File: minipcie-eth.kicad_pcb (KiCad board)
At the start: 2 copper layers, 156 x 41 mm, 36 parts, among them J2 POE PMOD, U1 VoCore_v2, U2 si3404, U3 ap2112, U4 MPCIE-Socket, X1 SI-52003-F

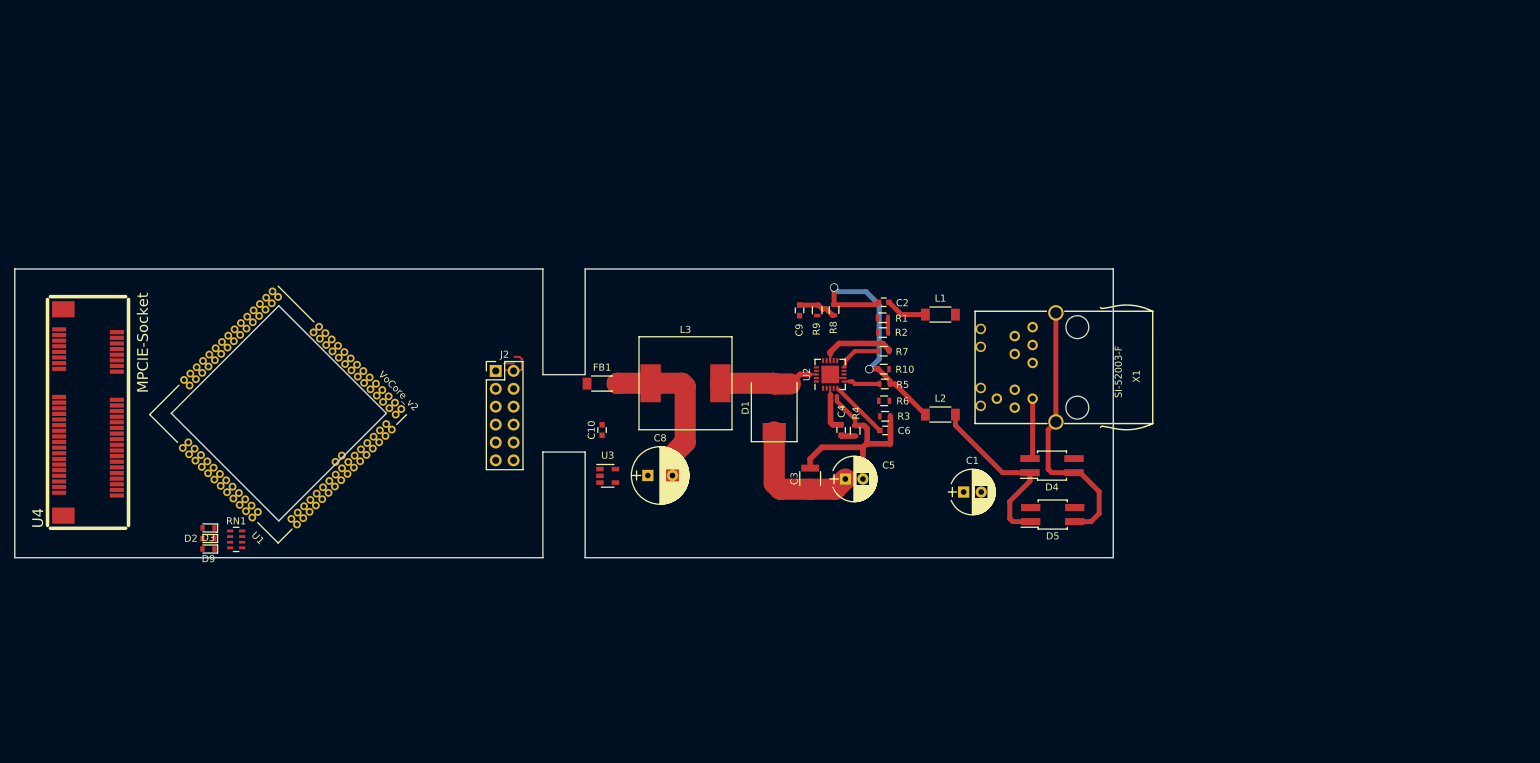
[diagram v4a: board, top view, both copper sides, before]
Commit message: Added PMOD 6 header pins, mouse bites, copper fills for main board
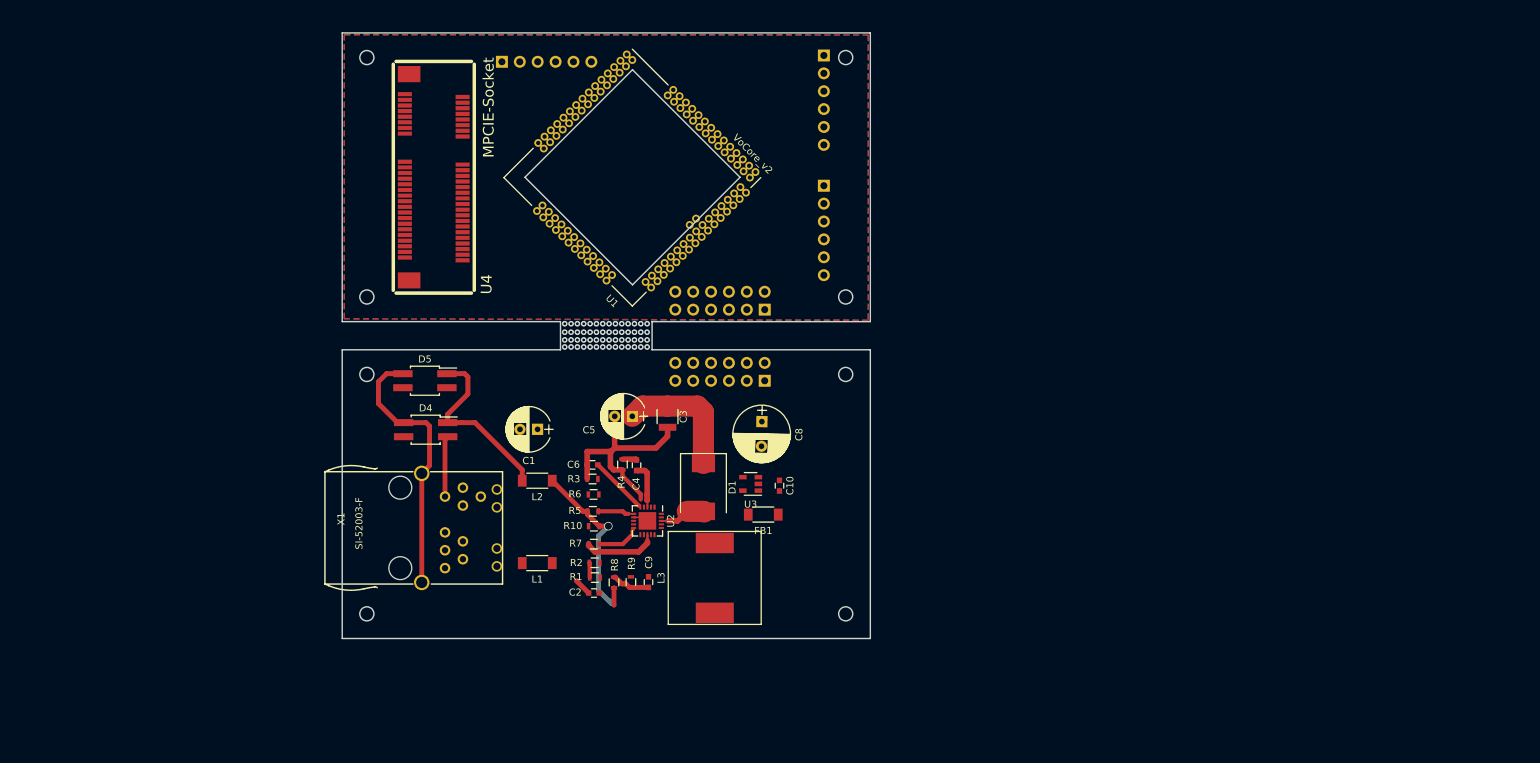
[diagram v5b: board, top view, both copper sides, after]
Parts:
- removed D2: TX, KiCad/Diodes_SMD.pretty:D_0603
- removed D3: PWR, KiCad/Diodes_SMD.pretty:D_0603
- removed D9: RX, KiCad/Diodes_SMD.pretty:D_0603
- removed RN1: RN_LEDS, KiCad/Resistors_SMD.pretty:R_Array_Concave_4x0603
- added J1: PoE connector MainBoard, Connector_PinHeader_2.54mm:PinHeader_2x06_P2.54mm_Vertical, B.Cu at (170.9, 86.7)
- added J3: PoE connector addon, Connector_PinHeader_2.54mm:PinHeader_2x06_P2.54mm_Vertical, B.Cu at (170.9, 96.8)
- added J4: PMOD UART 6pin, Connector_PinHeader_2.54mm:PinHeader_1x06_P2.54mm_Horizontal, B.Cu at (179.3, 50.6)
- added J5: PMOD UART 6pin, Connector_PinHeader_2.54mm:PinHeader_1x06_P2.54mm_Horizontal, B.Cu at (133.6, 51.5)
- J2: value POE PMOD -> PMOD I2C 6pin; footprint Connector_PinHeader_2.54mm:PinHeader_2x06_P2.54mm_Vertical -> Connector_PinHeader_2.54mm:PinHeader_1x06_P2.54mm_Horizontal; moved to B.Cu
- moved X1 92.9 mm to (122.2, 117.7), turned to 270 degrees
- moved D5 91.2 mm to (122.6, 96.8), turned to 0 degrees
- moved D4 89.1 mm to (122.7, 103.7), turned to 0 degrees
- moved L1 67.3 mm to (138.6, 122.7), turned to 180 degrees
- moved C1 61.2 mm to (138.6, 103.7), turned to 180 degrees
- moved U1 60.5 mm to (152.1, 68.0)
- moved U4 59.4 mm to (123.9, 55.4)
- moved C2 58.3 mm to (146.6, 126.9), turned to 180 degrees
- moved L2 58.0 mm to (138.6, 111.0), turned to 180 degrees
- moved R1 55.0 mm to (146.8, 124.7), turned to 180 degrees
- moved J2 53.5 mm to (179.3, 69.1), turned to 180 degrees
- moved R2 52.4 mm to (146.7, 122.6), turned to 180 degrees
- moved R8 49.7 mm to (149.5, 125.4), turned to 90 degrees
- moved R7 49.4 mm to (146.6, 120.0), turned to 180 degrees
- moved R10 46.8 mm to (146.6, 117.4), turned to 180 degrees
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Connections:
- C10 pad 1: +5V -> /ethernet + POE/5V+_POE
- C10 pad 2: GND -> /ethernet + POE/3V3-_POE
- C2 pad 1: +5V -> /ethernet + POE/5V+_POE
- C3 pad 1: +5V -> /ethernet + POE/5V+_POE
- C5 pad 1: +5V -> /ethernet + POE/5V+_POE
- C8 pad 1: +5V -> /ethernet + POE/5V+_POE
- C9 pad 2: GND -> /ethernet + POE/3V3-_POE
- D1 pad 1: +5V -> /ethernet + POE/5V+_POE
- FB1 pad 1: GND -> /ethernet + POE/3V3-_POE
- J2 pad 1: Net-(J2-Pad1) -> (no net)
- J2 pad 2: Net-(J2-Pad2) -> (no net)
- J2 pad 5: GNDA -> GND
- J2 pad 6: VBUS -> +3V3
- L2 pad 1: +5V -> /ethernet + POE/5V+_POE
- R10 pad 1: +5V -> /ethernet + POE/5V+_POE
- R10 pad 2: GND -> /ethernet + POE/3V3-_POE
- R5 pad 2: +5V -> /ethernet + POE/5V+_POE
- R8 pad 1: +5V -> /ethernet + POE/5V+_POE
- R9 pad 2: GND -> /ethernet + POE/3V3-_POE
- U1 pad 34: Net-(U1-Pad34) -> GND
- U1 pad 35: Net-(U1-Pad35) -> GND
- U1 pad 42: ETH_INGRESS_LED -> Net-(J4-Pad1)
- U1 pad 43: ETH_EGRESS_LED -> /minipcie/MCU_PROG
- U1 pad 44: Net-(U1-Pad44) -> /minipcie/MCU_RESET
- U1 pad 45: /minipcie/MCU_PROG -> Net-(J4-Pad2)
- U1 pad 46: /minipcie/MCU_RESET -> Net-(J4-Pad3)
- U1 pad 5: /ethernet + POE/PORP -> Net-(J1-Pad12)
- U1 pad 52: Net-(U1-Pad52) -> Net-(J2-Pad3)
- U1 pad 53: Net-(U1-Pad53) -> Net-(J2-Pad4)
- U1 pad 6: /ethernet + POE/PORN -> Net-(J1-Pad10)
- U1 pad 7: /ethernet + POE/POTP -> Net-(J1-Pad11)
- U1 pad 8: /ethernet + POE/POTN -> Net-(J1-Pad9)
- U3 pad 1: +5V -> /ethernet + POE/5V+_POE
- U3 pad 2: GND -> /ethernet + POE/3V3-_POE
- U3 pad 3: +5V -> /ethernet + POE/5V+_POE
- U3 pad 5: +3V3 -> /ethernet + POE/3V3+_POE
- U4 pad 42: /minipcie/TX_LED -> (no net)
- U4 pad 44: /minipcie/RX_LED -> (no net)
- X1 pad A1: ETH_INGRESS_LED -> /ethernet + POE/LED2
- X1 pad A2: ETH_EGRESS_LED -> /ethernet + POE/LED1
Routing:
- net +5V: track 57.4 -> 0.00 mm, vias 2 -> 0
- net /ethernet + POE/5V+_POE: track 0.00 -> 47.0 mm, vias 0 -> 1
- net Net-(C8-Pad2): track 23.3 -> 0.00 mm
- net Net-(D1-Pad2): track 14.6 -> 7.04 mm
- net Net-(J2-Pad2): track 5.02 -> 0.00 mm
- net Net-(C2-Pad2): track 11.0 -> 7.62 mm
- net GND: track 1.45 -> 0.00 mm
- net (no net): vias 0 -> 56
- added copper zone on F.Cu, net +3V3
- added copper zone on B.Cu, net GND
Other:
- board size 156 x 41 mm -> 75 x 86 mm

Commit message: Initial 2-layer board routing proves unfeasible, switching to 4-layer design instead
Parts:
- moved J3 4.80 mm to (175.7, 96.8)
- moved J1 4.72 mm to (175.6, 86.3)
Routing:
- net /minipcie/USB_D+: track 0.00 -> 71.0 mm
- net /minipcie/USB_D-: track 0.00 -> 68.1 mm
- net GND: track 0.00 -> 39.7 mm, vias 0 -> 12
- net /minipcie/SPI_CLK: track 0.00 -> 38.3 mm, vias 0 -> 1
- net /minipcie/SPI_MOSI: track 0.00 -> 33.8 mm
- net /minipcie/SPI_MISO: track 0.00 -> 32.8 mm, vias 0 -> 1
- net /minipcie/SPI_CS: track 0.00 -> 32.7 mm
- net /minipcie/MCU_RESET: track 0.00 -> 17.6 mm
- net /minipcie/RF_KILL: track 0.00 -> 16.5 mm, vias 0 -> 1
- net Net-(J5-Pad2): track 0.00 -> 12.2 mm
- net Net-(J5-Pad3): track 0.00 -> 10.7 mm
- net Net-(J5-Pad4): track 0.00 -> 8.69 mm
- net +3V3: track 0.00 -> 6.32 mm, vias 0 -> 3
- net +5V: track 0.00 -> 4.77 mm
- net Net-(U1-Pad23): track 0.00 -> 1.12 mm
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
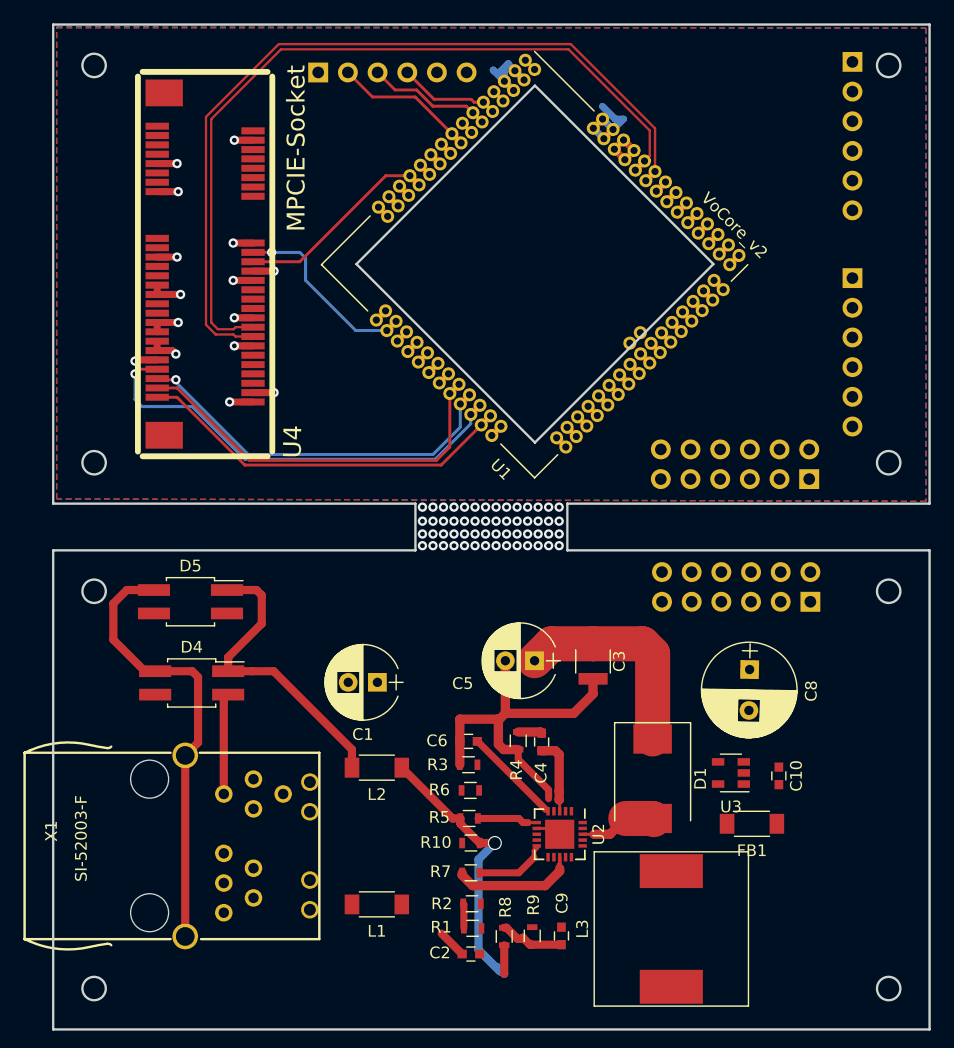
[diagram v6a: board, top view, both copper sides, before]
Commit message: Mainboard routing finished with 4 layers. Status update sent to n-fuse
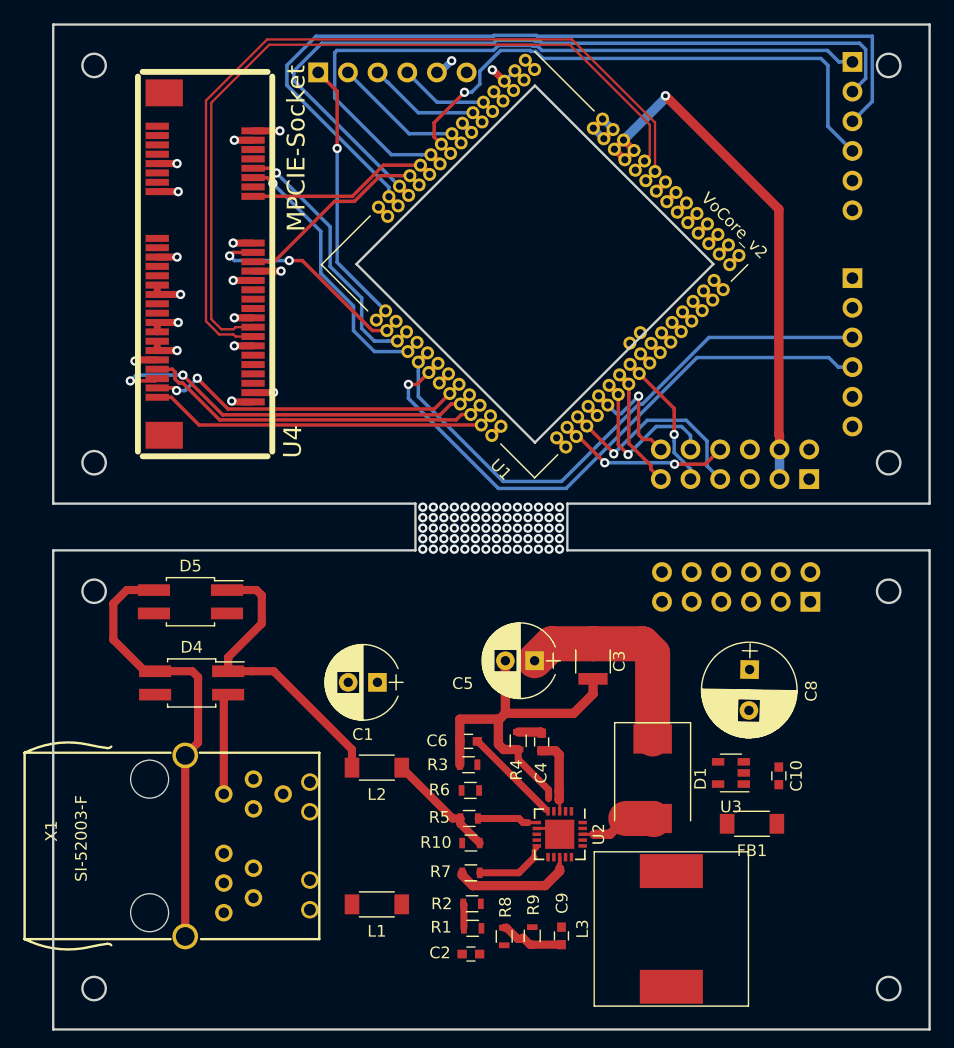
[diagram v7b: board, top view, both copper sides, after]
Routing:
- net Net-(J4-Pad3): track 1.12 -> 75.1 mm
- net Net-(J4-Pad2): track 1.12 -> 69.1 mm
- net Net-(J4-Pad1): track 1.12 -> 60.4 mm
- net Net-(J2-Pad4): track 1.12 -> 50.7 mm, vias 0 -> 1
- net Net-(J2-Pad3): track 1.12 -> 49.3 mm
- net Net-(J4-Pad4): track 1.12 -> 47.7 mm, vias 0 -> 1
- net +5V: track 4.77 -> 46.9 mm, vias 0 -> 1
- net Net-(J5-Pad1): track 1.12 -> 23.9 mm, vias 0 -> 1
- net /minipcie/SWD_CLK: track 1.12 -> 23.9 mm, vias 0 -> 1
- net /minipcie/SWD_IO: track 1.12 -> 23.1 mm, vias 0 -> 1
- net Net-(J1-Pad7): track 1.12 -> 18.1 mm, vias 0 -> 1
- net /ethernet + POE/5V+_POE: track 47.0 -> 30.1 mm, vias 1 -> 0
- net /minipcie/MCU_PROG: track 1.12 -> 16.5 mm
- net Net-(J1-Pad8): track 1.12 -> 14.9 mm, vias 0 -> 2
- net Net-(J1-Pad10): track 1.12 -> 14.4 mm, vias 0 -> 1
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- added copper zone on In1.Cu, net +3V3
- added copper zone on In2.Cu, net GND
- removed copper zone on F.Cu, net +3V3
- removed copper zone on B.Cu, net GND
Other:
- copper layers 2 -> 4

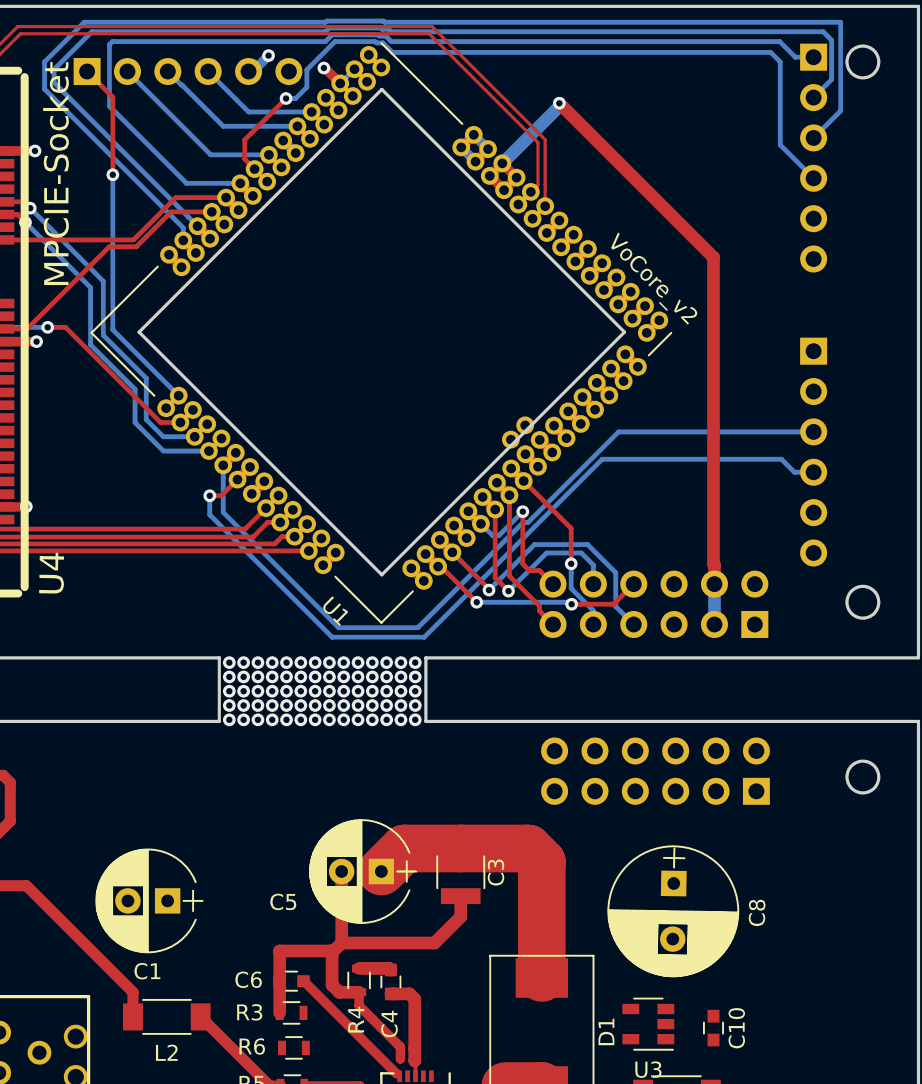
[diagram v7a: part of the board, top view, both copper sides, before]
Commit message: Decided, I will switch to isolated si34061 design since the power budget and isolation are a bit too tight on the si3404... might change it all with the TPS23750 (https://www.ti.com/lit/ds/symlink/tps23770.pdf) in the future though
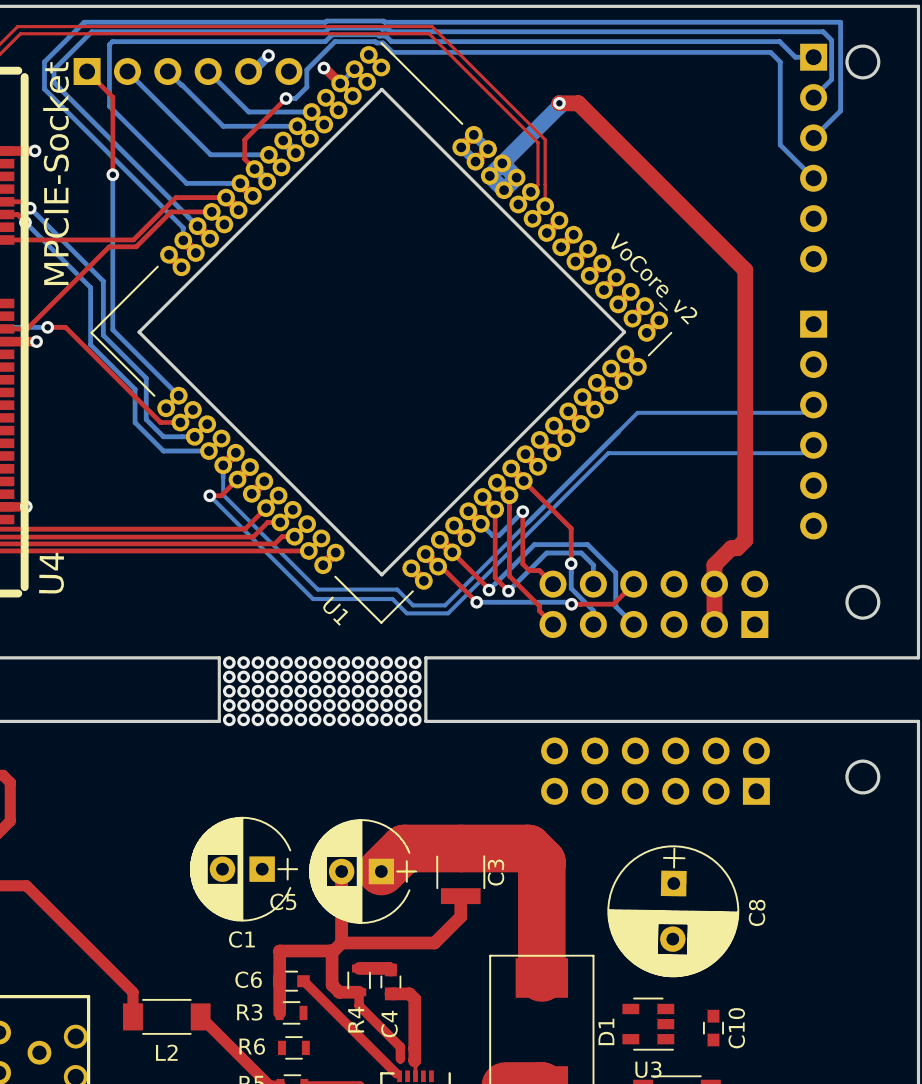
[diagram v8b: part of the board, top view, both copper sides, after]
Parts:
- moved C1 6.28 mm to (144.6, 101.7)
- moved J2 1.70 mm to (179.3, 67.4)
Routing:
- net +5V: track 46.9 -> 49.4 mm
- net Net-(J2-Pad3): track 49.3 -> 48.0 mm
- net Net-(J2-Pad4): track 50.7 -> 49.4 mm
- net Net-(J4-Pad4): track 47.7 -> 48.8 mm
